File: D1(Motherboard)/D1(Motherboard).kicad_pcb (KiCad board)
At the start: 4 copper layers, 38 x 35 mm, 82 parts, among them J1 WR-FPC_0.5mm_ZIF_V, J2 USB_C_Receptacle_USB2.0, J3 B2B-PH-K-S, Q1 NX2301P.215, Q2 MBT3904DW1, SW1 CHS-02A, U1 CP2102N-A01-GQFN28, U2 ICM-20602, U3 WR-FPC_0.5mm_ZIF_H, U4 MIC5353-3.3YMT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

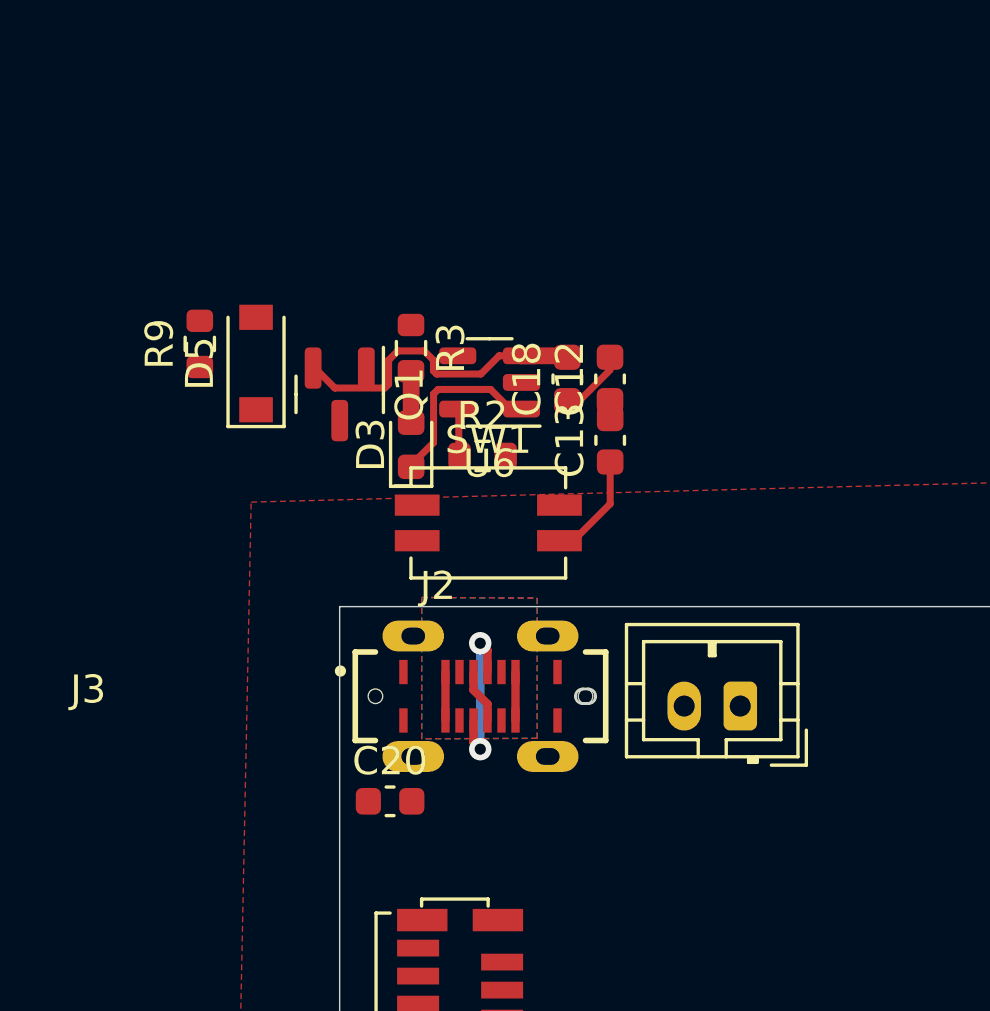
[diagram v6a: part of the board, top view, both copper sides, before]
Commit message: Small update moving load sharing circuit, need to check voltage references
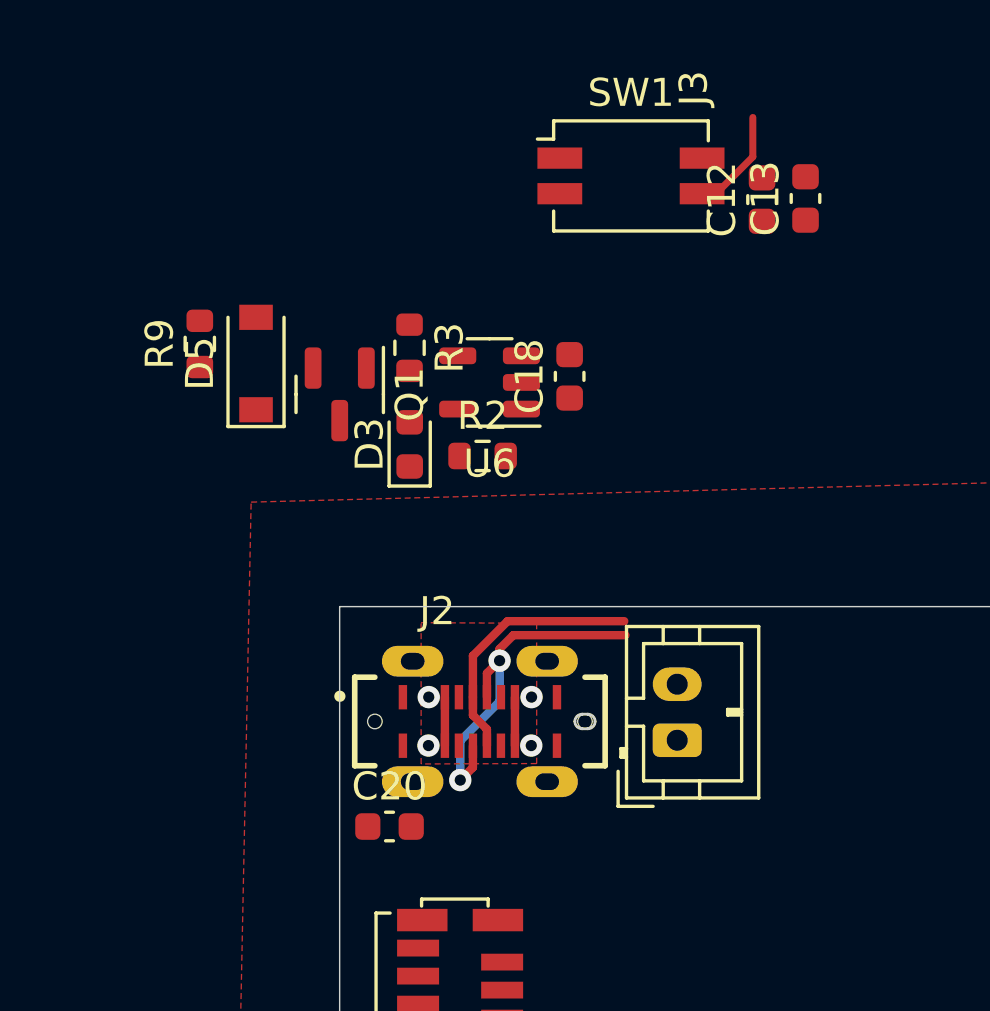
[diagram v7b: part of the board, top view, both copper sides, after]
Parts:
- moved SW1 13.4 mm to (44.0, 16.5)
- moved C13 11.1 mm to (50.3, 17.3)
- moved C12 8.39 mm to (48.7, 17.3)
- moved J3 2.56 mm to (45.7, 36.6), turned to 90 degrees
- moved J2 0.90 mm to (38.6, 35.9)
- moved C20 0.90 mm to (35.4, 39.7)
- moved C18 0.12 mm to (41.8, 23.6)
- moved R3 0.05 mm to (36.1, 22.6)
- moved D3 0.05 mm to (36.1, 26.0)
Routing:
- net +BATT: track 11.2 -> 0.00 mm
- net D+: track 3.92 -> 11.3 mm
- net D-: track 7.64 -> 14.5 mm
- net Net-(D3-Pad1): track 5.96 -> 0.00 mm
- net Net-(D3-Pad2): track 1.66 -> 0.00 mm
- net GND: track 10.8 -> 9.14 mm
- net Net-(R2-Pad1): track 1.61 -> 0.00 mm
- net VBUS: vias 0 -> 4
- added copper zone on In1.Cu, net VBUS
- removed copper zone on B.Cu, net VBUS

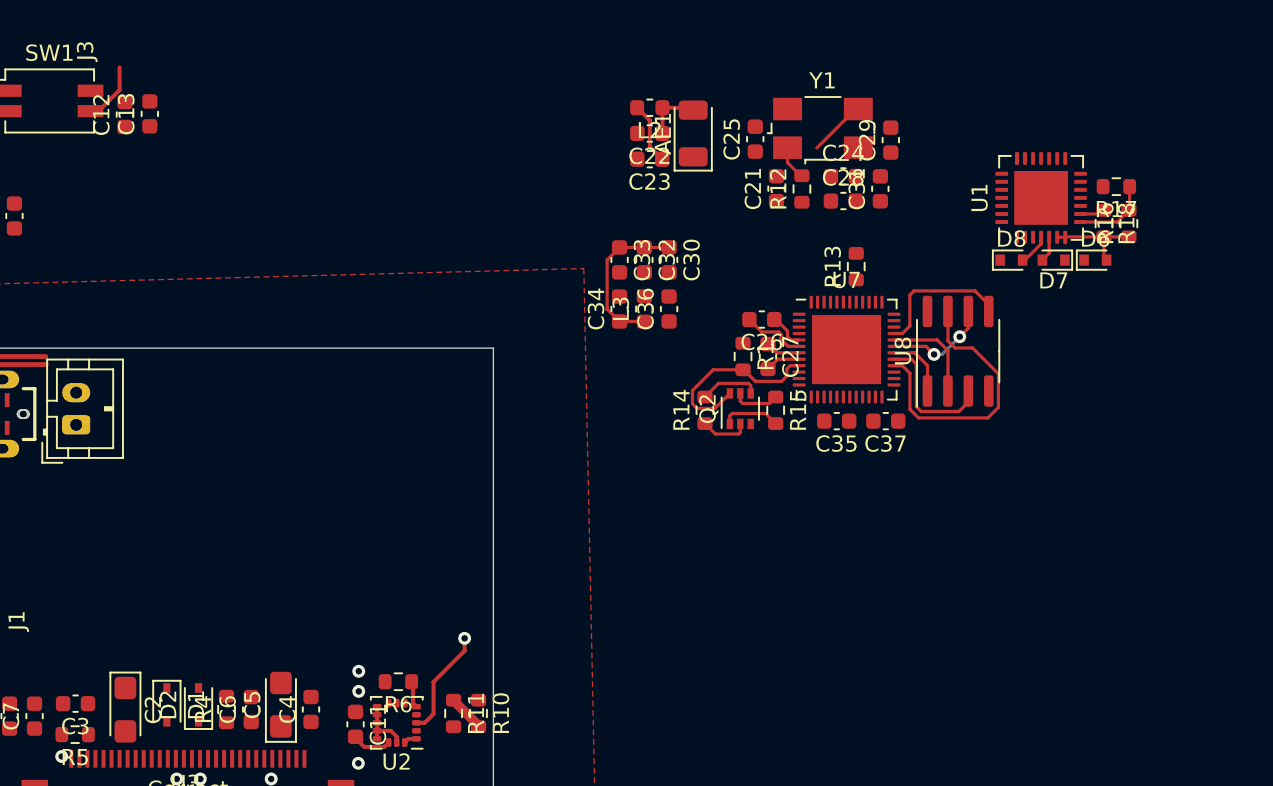
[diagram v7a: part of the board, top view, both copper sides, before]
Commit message: Fixed ignion antenna, and added some more to the esp32-s2 schematic
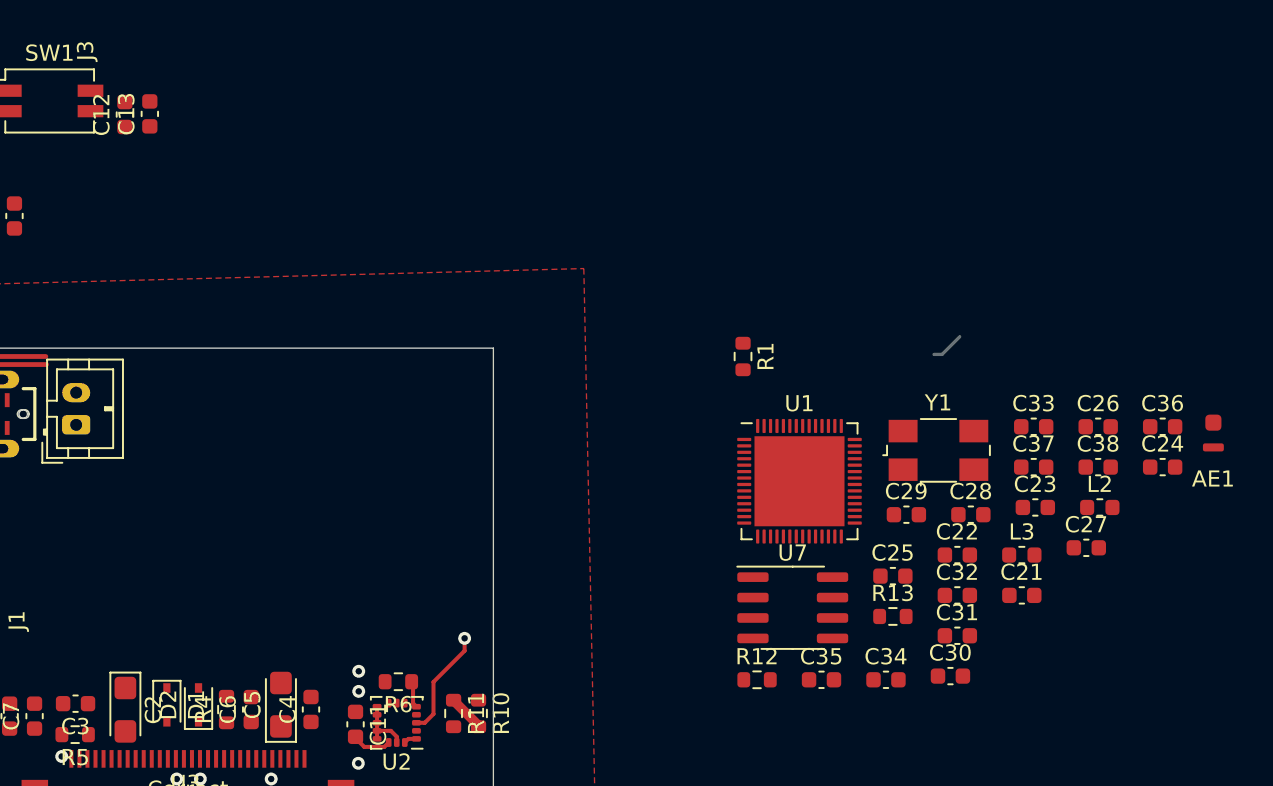
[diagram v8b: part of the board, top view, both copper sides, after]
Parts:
- removed D6, D7, D8: ESD5B5.0S, Diode_SMD:D_SOD-523
- removed Q2: MBT3904DW1, Package_TO_SOT_SMD:SOT-363_SC-70-6
- removed R14, R15: 10k, Resistor_SMD:R_0603_1608Metric
- removed R16: 22.1k, Resistor_SMD:R_0603_1608Metric
- removed R17: 47.5k, Resistor_SMD:R_0603_1608Metric
- removed R18: 1k, Resistor_SMD:R_0603_1608Metric
- removed U8: AT25SF081-SSHD-X, Package_SO:SOIC-8_3.9x4.9mm_P1.27mm
- added C38: 1u, Capacitor_SMD:C_0603_1608Metric, F.Cu at (109.2, 39.2)
- AE1: footprint RF_Antenna:Johanson_2450AT18x100 -> Ignion_Antenna:NN02-101
- C22: value TBD -> 10u
- C23: value TBD -> 1u
- C24: value 100pF -> 0.1u
- C25: value TBD -> 0.1u
- C26: value 270p -> TBD
- C27: value 270p -> 0.1u
- C28: value 1uF -> 270p
- C29: value TBD -> 270p
- C30: value 10u -> 1uF
- C31: value 0.1u -> 100pF
- C32: value NC -> 1uF
- C33, C37: value 1u -> TBD
- C34: value 0.1u -> TBD
- C36: value NC -> TBD
- L2: value TBD -> 2n
- L3: value 2n -> TBD
- U1: value CP2102N-A01-GQFN28 -> ESP32-S2; footprint Package_DFN_QFN:QFN-28-1EP_5x5mm_P0.5mm_EP3.35x3.35mm -> Package_DFN_QFN:QFN-56-1EP_7x7mm_P0.4mm_EP5.6x5.6mm
- U7: value ESP32-D0WDQ6-V3 -> AT25SF081-SSHD-X; footprint Package_DFN_QFN:QFN-48-1EP_6x6mm_P0.4mm_EP4.3x4.3mm -> Package_SO:SOIC-8_3.9x4.9mm_P1.27mm
- moved L2 37.4 mm to (109.3, 41.7), turned to 0 degrees
- moved AE1 37.4 mm to (116.4, 37.3), turned to 0 degrees
- moved C22 32.5 mm to (100.5, 44.7), turned to 0 degrees
- moved C23 32.3 mm to (105.3, 41.7), turned to 0 degrees
- moved C36 31.6 mm to (113.3, 36.7), turned to 0 degrees
- moved C30 31.2 mm to (100.1, 52.2), turned to 0 degrees
- moved R12 30.7 mm to (88.0, 52.5), turned to 0 degrees
- moved C21 29.5 mm to (104.5, 47.2), turned to 0 degrees
- moved C32 28.5 mm to (100.5, 47.2), turned to 0 degrees
- moved C25 28.5 mm to (96.5, 46.0), turned to 0 degrees
- moved C34 28.4 mm to (96.0, 52.5), turned to 0 degrees
- moved C31 28.2 mm to (100.5, 49.7), turned to 0 degrees
- moved L3 28.0 mm to (104.5, 44.7), turned to 0 degrees
- moved C33 27.8 mm to (105.2, 36.7), turned to 0 degrees
- moved C24 26.9 mm to (113.3, 39.2)
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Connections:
- C10 pad 2: +3V3 -> VDD3P3_CPU
- C17 pad 2: +3V3 -> VDD3P3_CPU
- C2 pad 1: +3V3 -> VDD3P3_CPU
- C21 pad 1: +3V3 -> VDD3P3_CPU
- C22 pad 1: Net-(AE1-Pad2) -> VDD3P3_CPU
- C23 pad 1: Net-(C23-Pad1) -> VDD3P3_CPU
- C24 pad 1: +3V3 -> VDD3P3_CPU
- C25 pad 1: GND -> VDD3P3_CPU
- C25 pad 2: Net-(C25-Pad2) -> GND
- C26 pad 1: Net-(C26-Pad1) -> VDD3P3
- C26 pad 2: Net-(C26-Pad2) -> GND
- C27 pad 1: Net-(C27-Pad1) -> VDD_SPI
- C27 pad 2: Net-(C27-Pad2) -> GND
- C28 pad 1: +3V3 -> unconnected-(C28-Pad1)
- C28 pad 2: GND -> unconnected-(C28-Pad2)
- C29 pad 1: GND -> unconnected-(C29-Pad1)
- C29 pad 2: XTAL_N -> unconnected-(C29-Pad2)
- C3 pad 2: +3V3 -> VDD3P3_CPU
- C30 pad 1: +3V3 -> VDD_SPI
- C31 pad 1: +3V3 -> VDD3P3_CPU
- C32 pad 1: +3V3 -> VDD3P3_CPU
- C33 pad 1: +3V3 -> Net-(AE1-Pad2)
- C34 pad 1: +3V3 -> LNA_IN
- C35 pad 1: +3V3 -> VDD3P3_CPU
- C36 pad 1: VDD3P3 -> GND
- C36 pad 2: GND -> XTAL_N
- C37 pad 1: VDD_SDIO -> GND
- C37 pad 2: GND -> Net-(C37-Pad2)
- C6 pad 1: +3V3 -> VDD3P3_CPU
- C9 pad 2: +3V3 -> VDD3P3_CPU
- J1 pad 11: +3V3 -> VDD3P3_CPU
- J1 pad 13: +3V3 -> VDD3P3_CPU
- J1 pad 9: +3V3 -> VDD3P3_CPU
- L2 pad 1: Net-(AE1-Pad2) -> VDD3P3_CPU
- L2 pad 2: Net-(C23-Pad1) -> VDD3P3
- L3 pad 1: +3V3 -> Net-(AE1-Pad2)
- L3 pad 2: VDD3P3 -> LNA_IN
- R1 pad 1: +3V3 -> VDD3P3_CPU
- R10 pad 2: /ESP32-D0WDQ6-V3/IO33 -> Net-(R10-Pad2)
- R11 pad 1: /ESP32-D0WDQ6-V3/IO33 -> Net-(R10-Pad2)
- R12 pad 2: Net-(C25-Pad2) -> Net-(C37-Pad2)
- R13 pad 1: Net-(R13-Pad1) -> unconnected-(R13-Pad1)
- R13 pad 2: TXD0 -> unconnected-(R13-Pad2)
- U1 pad 1: unconnected-(U1-Pad1) -> VDD3P3_CPU
- U1 pad 2: unconnected-(U1-Pad2) -> LNA_IN
- U1 pad 20: unconnected-(U1-Pad20) -> VDD3P3_CPU
- U1 pad 24: RTS -> unconnected-(U1-Pad24)
- U1 pad 25: RX -> unconnected-(U1-Pad25)
- U1 pad 26: TX -> unconnected-(U1-Pad26)
- U1 pad 28: DTR -> unconnected-(U1-Pad28)
- U1 pad 29: GND -> unconnected-(U1-Pad29)
- U1 pad 3: GND -> VDD3P3
- U1 pad 4: D+ -> VDD3P3
- U1 pad 5: D- -> unconnected-(U1-Pad5)
- U1 pad 6: VBUS -> Net-(R10-Pad2)
- U1 pad 7: VBUS -> unconnected-(U1-Pad7)
- U1 pad 8: Net-(R16-Pad2) -> unconnected-(U1-Pad8)
- U1 pad 9: Net-(R18-Pad1) -> unconnected-(U1-Pad9)
- U2 pad 1: +3V3 -> VDD3P3_CPU
- U2 pad 16: +3V3 -> VDD3P3_CPU
- U3 pad 4: +3V3 -> VDD3P3_CPU
- U4 pad 4: +3V3 -> VDD3P3_CPU
- U7 pad 1: +3V3 -> SCS/CMD
- U7 pad 2: Net-(C23-Pad1) -> SDO/SD0
- U7 pad 3: VDD3P3 -> SWP/SD3
- U7 pad 4: VDD3P3 -> GND
- U7 pad 5: Net-(C26-Pad1) -> SDI/SD1
- U7 pad 6: Net-(C26-Pad2) -> SCK/CLK
- U7 pad 7: Net-(C27-Pad1) -> SHD/SD2
- U7 pad 8: Net-(C27-Pad2) -> VDD_SDIO
- Y1 pad 1: Net-(C25-Pad2) -> Net-(C37-Pad2)
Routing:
- net /ESP32-D0WDQ6-V3/SHD/SD2: track 17.3 -> 0.00 mm
- net +3V3: track 15.5 -> 0.00 mm, vias 3 -> 0
- net Reset: track 15.5 -> 0.50 mm
- net /ESP32-D0WDQ6-V3/SDI/SD1: track 8.89 -> 0.00 mm
- net /ESP32-D0WDQ6-V3/SWP/SD3: track 8.46 -> 0.00 mm
- net /ESP32-D0WDQ6-V3/SCK/CLK: track 6.55 -> 0.00 mm, vias 2 -> 0
- net VBUS: track 9.79 -> 3.46 mm
- net /ESP32-D0WDQ6-V3/SDO/SD0: track 6.14 -> 0.00 mm
- net VDD3P3_CPU: track 0.00 -> 5.64 mm, vias 0 -> 3
- net Net-(R16-Pad2): track 4.80 -> 0.00 mm
- net /ESP32-D0WDQ6-V3/SCS/CMD: track 3.99 -> 0.00 mm
- net Net-(C26-Pad2): track 3.97 -> 0.00 mm
- net Net-(C23-Pad1): track 3.85 -> 0.00 mm
- net DTR: track 3.74 -> 0.00 mm
- net RTS: track 3.67 -> 0.00 mm
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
